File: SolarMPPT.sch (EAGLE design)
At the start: 31 parts, among them J1 CORTEX_DEBUG_SMD, U1 STM32F091CCT6, U3 LTC1155, U4 LM22674MRX-5.0, U5 3.3V

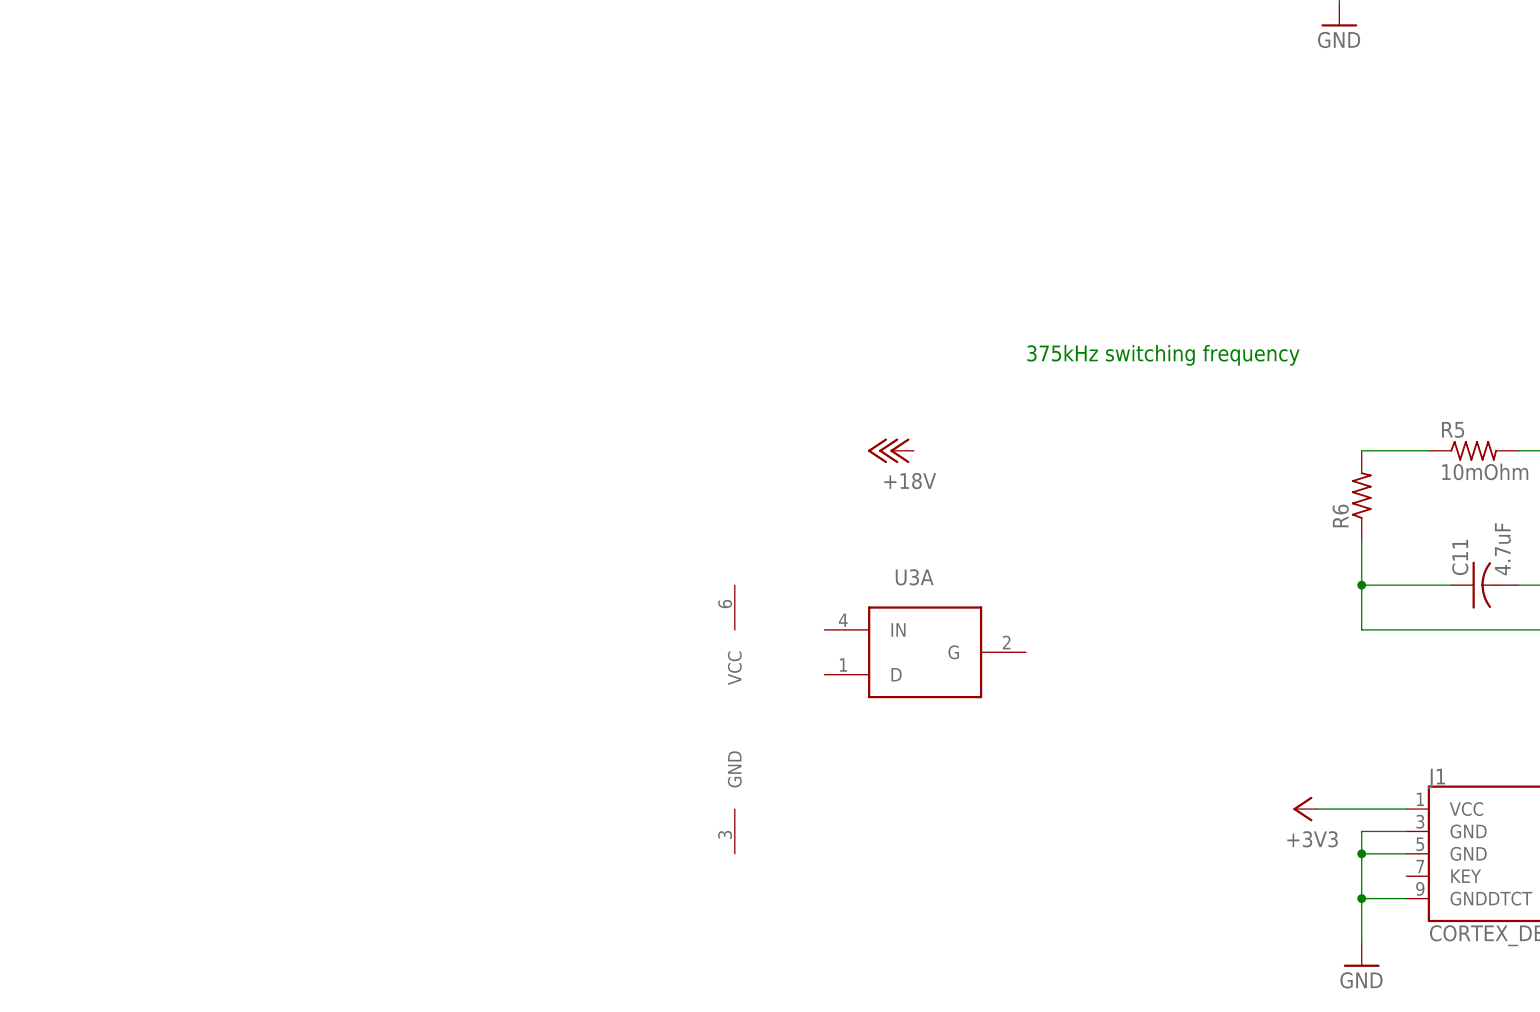
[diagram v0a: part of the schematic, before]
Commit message: Added LT1255 gate driver and MOSFETs
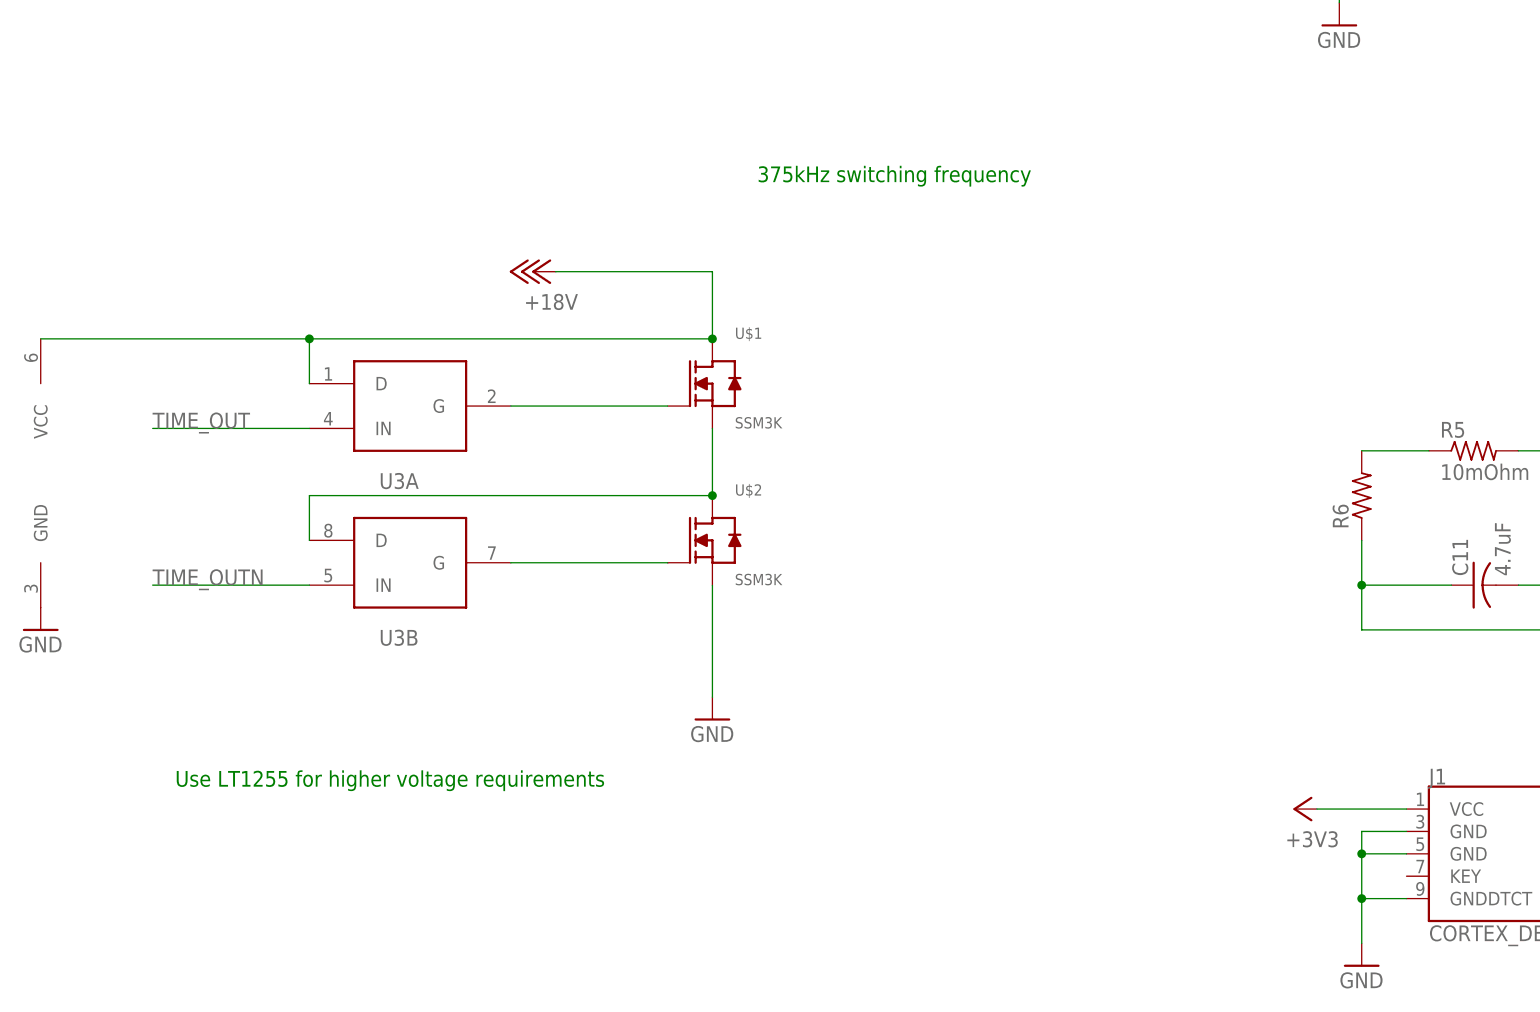
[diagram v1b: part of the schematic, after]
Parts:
- added U$1, U$2: SSM3K, FormE:SSM3K
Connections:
- new net N$4: U$1.G, U3A.G
- new net N$7: U$1.S, U$2.D, U3B.D
- new net N$8: U$2.G, U3B.G
- new net TIME_OUTN: U3B.IN
- net +18V: now also U$1.D, U3A.D, U3P.VCC
- net GND: now also U$2.S, U3P.GND
- net TIME_OUT: now also U3A.IN
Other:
- note added: "Use LT1255 for higher voltage requirements"
- moved on the sheet: U3A
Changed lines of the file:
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@@
 <part name="+3V13" library="supply1" library_urn="urn:adsk.eagle:library:371" deviceset="+3V3" device=""/>
 <part name="P+5" library="supply1" library_urn="urn:adsk.eagle:library:371" deviceset="+12V" device=""/>
+<part name="U$1" library="FormE" deviceset="SSM3K" device=""/>
+<part name="U$2" library="FormE" deviceset="SSM3K" device=""/>
+<part name="GND16" library="supply1" library_urn="urn:adsk.eagle:library:371" deviceset="GND" device=""/>
+<part name="GND18" library="supply1" library_urn="urn:adsk.eagle:library:371" deviceset="GND" device=""/>
 </parts>
 <sheets>
@@
 <text x="71.12" y="132.08" size="1.778" layer="91">.08Hz</text>
 <text x="12.7" y="162.56" size="1.778" layer="91">100V/V, 1V/A</text>
-<text x="-91.44" y="177.8" size="1.778" layer="91">375kHz switching frequency</text>
+<text x="-121.92" y="198.12" size="1.778" layer="91">375kHz switching frequency</text>
 <text x="2.54" y="233.68" size="1.778" layer="97" rot="MR0">SDR1105-151KL</text>
 <text x="-73.66" y="228.6" size="1.778" layer="97" rot="MR0">NC</text>
+<text x="-187.96" y="129.54" size="1.778" layer="91">Use LT1255 for higher voltage requirements</text>
 </plain>
 <instances>
@@
 <attribute name="VALUE" x="-17.78" y="170.18" size="1.778" layer="96"/>
 </instance>
-<instance part="P+4" gate="1" x="-106.68" y="167.64" smashed="yes" rot="R90">
-<attribute name="VALUE" x="-101.6" y="165.1" size="1.778" layer="96" rot="R180"/>
+<instance part="P+4" gate="1" x="-147.32" y="187.96" smashed="yes" rot="R90">
+<attribute name="VALUE" x="-142.24" y="185.42" size="1.778" layer="96" rot="R180"/>
 </instance>
 <instance part="R5" gate="G$1" x="-40.64" y="167.64" smashed="yes">
@@
 <attribute name="VALUE" x="30.48" y="144.78" size="1.778" layer="96"/>
 </instance>
-<instance part="U3" gate="A" x="-104.14" y="144.78" smashed="yes">
-<attribute name="NAME" x="-104.14" y="152.4" size="1.778" layer="95" font="vector" align="bottom-center"/>
-</instance>
-<instance part="U3" gate="P" x="-124.46" y="137.16" smashed="yes"/>
+<instance part="U3" gate="A" x="-162.56" y="172.72" smashed="yes" rot="MR180">
+<attribute name="NAME" x="-162.56" y="165.1" size="1.778" layer="95" font="vector" rot="MR180" align="bottom-center"/>
+</instance>
+<instance part="U3" gate="P" x="-203.2" y="165.1" smashed="yes"/>
 <instance part="P+15" gate="1" x="12.7" y="236.22" smashed="yes">
 <attribute name="VALUE" x="10.16" y="231.14" size="1.778" layer="96" rot="R90"/>
@@
 <instance part="P+5" gate="1" x="-99.06" y="254" smashed="yes">
 <attribute name="VALUE" x="-101.6" y="248.92" size="1.778" layer="96" rot="R90"/>
+</instance>
+<instance part="U3" gate="B" x="-162.56" y="154.94" smashed="yes" rot="MR180">
+<attribute name="NAME" x="-162.56" y="147.32" size="1.778" layer="95" font="vector" rot="MR180" align="bottom-center"/>
+</instance>
+<instance part="U$1" gate="G$1" x="-127" y="172.72" smashed="yes">
+<attribute name="NAME" x="-124.46" y="180.34" size="1.27" layer="95"/>
+<attribute name="VALUE" x="-124.46" y="170.18" size="1.27" layer="96"/>
+</instance>
+<instance part="U$2" gate="G$1" x="-127" y="154.94" smashed="yes">
+<attribute name="NAME" x="-124.46" y="162.56" size="1.27" layer="95"/>
+<attribute name="VALUE" x="-124.46" y="152.4" size="1.27" layer="96"/>
+</instance>
+<instance part="GND16" gate="1" x="-127" y="137.16" smashed="yes">
+<attribute name="VALUE" x="-129.54" y="134.62" size="1.778" layer="96"/>
+</instance>
+<instance part="GND18" gate="1" x="-203.2" y="147.32" smashed="yes">
+<attribute name="VALUE" x="-205.74" y="144.78" size="1.778" layer="96"/>
 </instance>
 </instances>
@@
 <junction x="12.7" y="215.9"/>
 </segment>
+<segment>
+<pinref part="U$2" gate="G$1" pin="S"/>
+<pinref part="GND16" gate="1" pin="GND"/>
+<wire x1="-127" y1="152.4" x2="-127" y2="139.7" width="0.1524" layer="91"/>
+</segment>
+<segment>
+<pinref part="U3" gate="P" pin="GND"/>
+<pinref part="GND18" gate="1" pin="GND"/>
+</segment>
 </net>
 <net name="N$1" class="0">
@@
 <wire x1="101.6" y1="139.7" x2="101.6" y2="137.16" width="0.1524" layer="91"/>
 </segment>
+<segment>
+<pinref part="P+4" gate="1" pin="+18V"/>
+<pinref part="U$1" gate="G$1" pin="D"/>
+<wire x1="-144.78" y1="187.96" x2="-127" y2="187.96" width="0.1524" layer="91"/>
+<wire x1="-127" y1="187.96" x2="-127" y2="180.34" width="0.1524" layer="91"/>
+<pinref part="U3" gate="A" pin="D"/>
+<wire x1="-172.72" y1="175.26" x2="-172.72" y2="180.34" width="0.1524" layer="91"/>
+<wire x1="-172.72" y1="180.34" x2="-127" y2="180.34" width="0.1524" layer="91"/>
+<junction x="-127" y="180.34"/>
+<pinref part="U3" gate="P" pin="VCC"/>
+<wire x1="-203.2" y1="180.34" x2="-172.72" y2="180.34" width="0.1524" layer="91"/>
+<junction x="-172.72" y="180.34"/>
+</segment>
 </net>
 <net name="SOLAR_SENS" class="0">
@@
 <wire x1="22.86" y1="101.6" x2="22.86" y2="119.38" width="0.1524" layer="91"/>
 <label x="22.86" y="106.68" size="1.778" layer="95" rot="R90"/>
+</segment>
+<segment>
+<pinref part="U3" gate="A" pin="IN"/>
+<wire x1="-172.72" y1="170.18" x2="-190.5" y2="170.18" width="0.1524" layer="91"/>
+<label x="-190.5" y="170.18" size="1.778" layer="95"/>
 </segment>
 </net>
@@
 </segment>
 </net>
+<net name="N$4" class="0">
+<segment>
+<pinref part="U3" gate="A" pin="G"/>
+<pinref part="U$1" gate="G$1" pin="G"/>
+<wire x1="-149.86" y1="172.72" x2="-132.08" y2="172.72" width="0.1524" layer="91"/>
+</segment>
+</net>
+<net name="N$7" class="0">
+<segment>
+<pinref part="U$1" gate="G$1" pin="S"/>
+<pinref part="U$2" gate="G$1" pin="D"/>
+<wire x1="-127" y1="170.18" x2="-127" y2="162.56" width="0.1524" layer="91"/>
+<pinref part="U3" gate="B" pin="D"/>
+<wire x1="-172.72" y1="157.48" x2="-172.72" y2="162.56" width="0.1524" layer="91"/>
+<wire x1="-172.72" y1="162.56" x2="-127" y2="162.56" width="0.1524" layer="91"/>
+<junction x="-127" y="162.56"/>
+</segment>
+</net>
+<net name="N$8" class="0">
+<segment>
+<pinref part="U$2" gate="G$1" pin="G"/>
+<pinref part="U3" gate="B" pin="G"/>
+<wire x1="-132.08" y1="154.94" x2="-149.86" y2="154.94" width="0.1524" layer="91"/>
+</segment>
+</net>
+<net name="TIME_OUTN" class="0">
+<segment>
+<pinref part="U3" gate="B" pin="IN"/>
+<wire x1="-172.72" y1="152.4" x2="-190.5" y2="152.4" width="0.1524" layer="91"/>
+<label x="-190.5" y="152.4" size="1.778" layer="95"/>
+</segment>
+</net>
